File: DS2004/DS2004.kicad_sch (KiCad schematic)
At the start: 24 parts, among them U1 plot_i2, U2 plot_i2, U3 plot_i2, U4 plot_i2, U5 plot_i2, U6 plot_i2, U7 plot_i2, U8 plot_i2, X1 DS2004

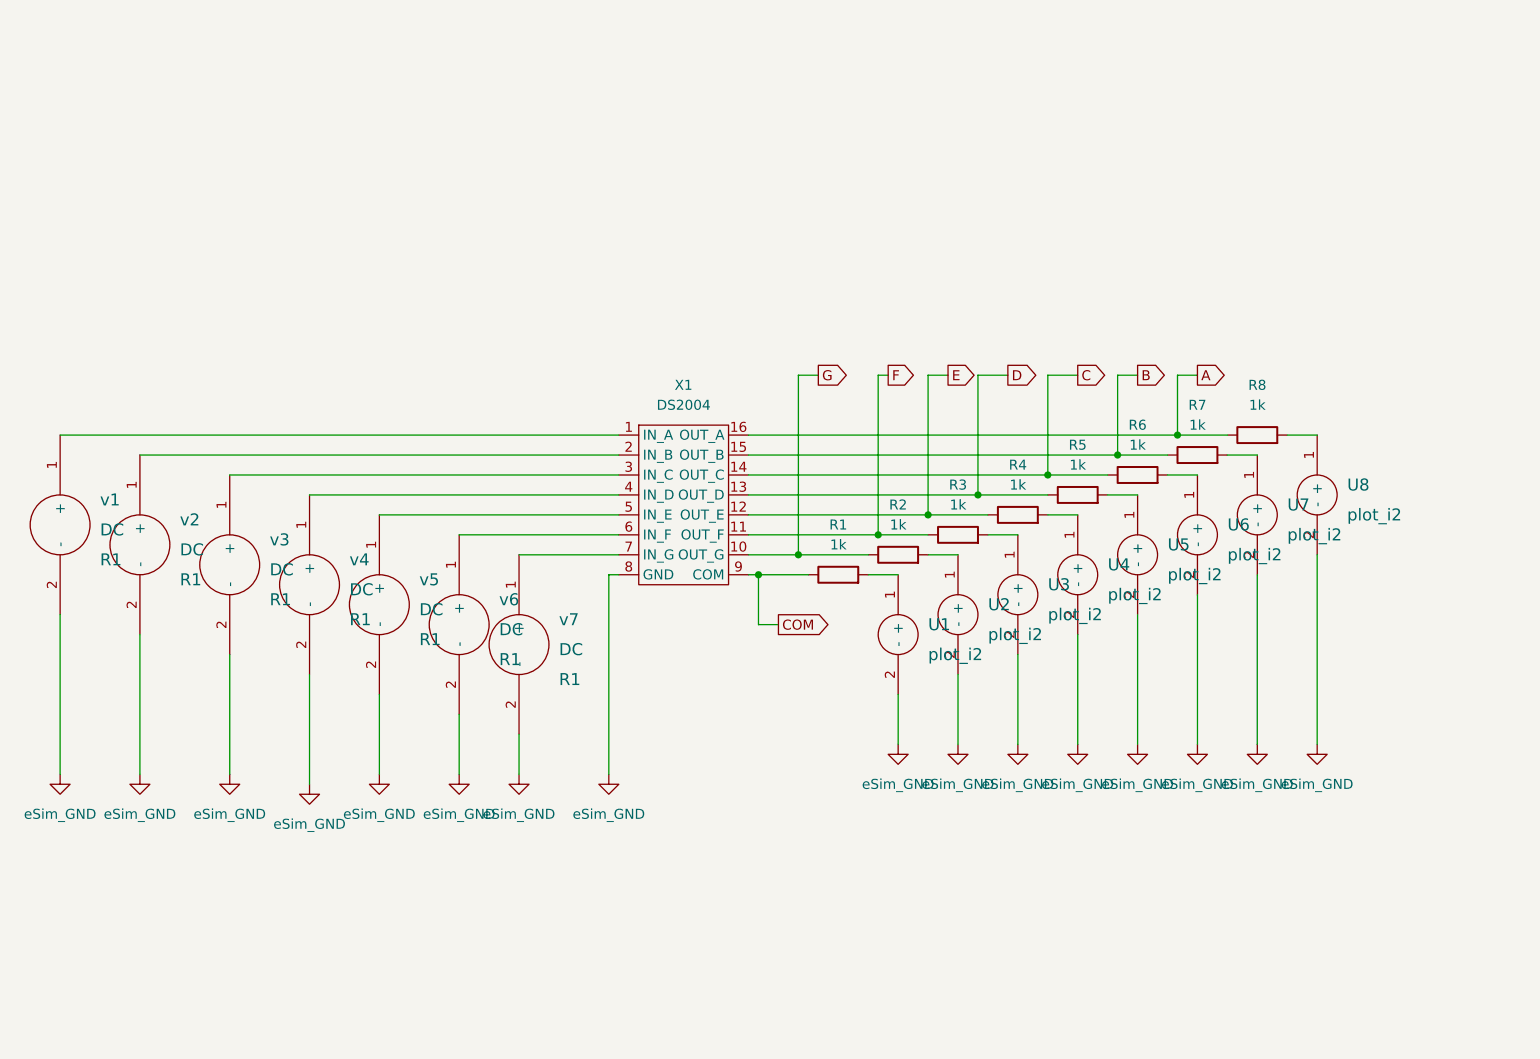
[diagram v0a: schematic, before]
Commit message: IC circuit of DS2004
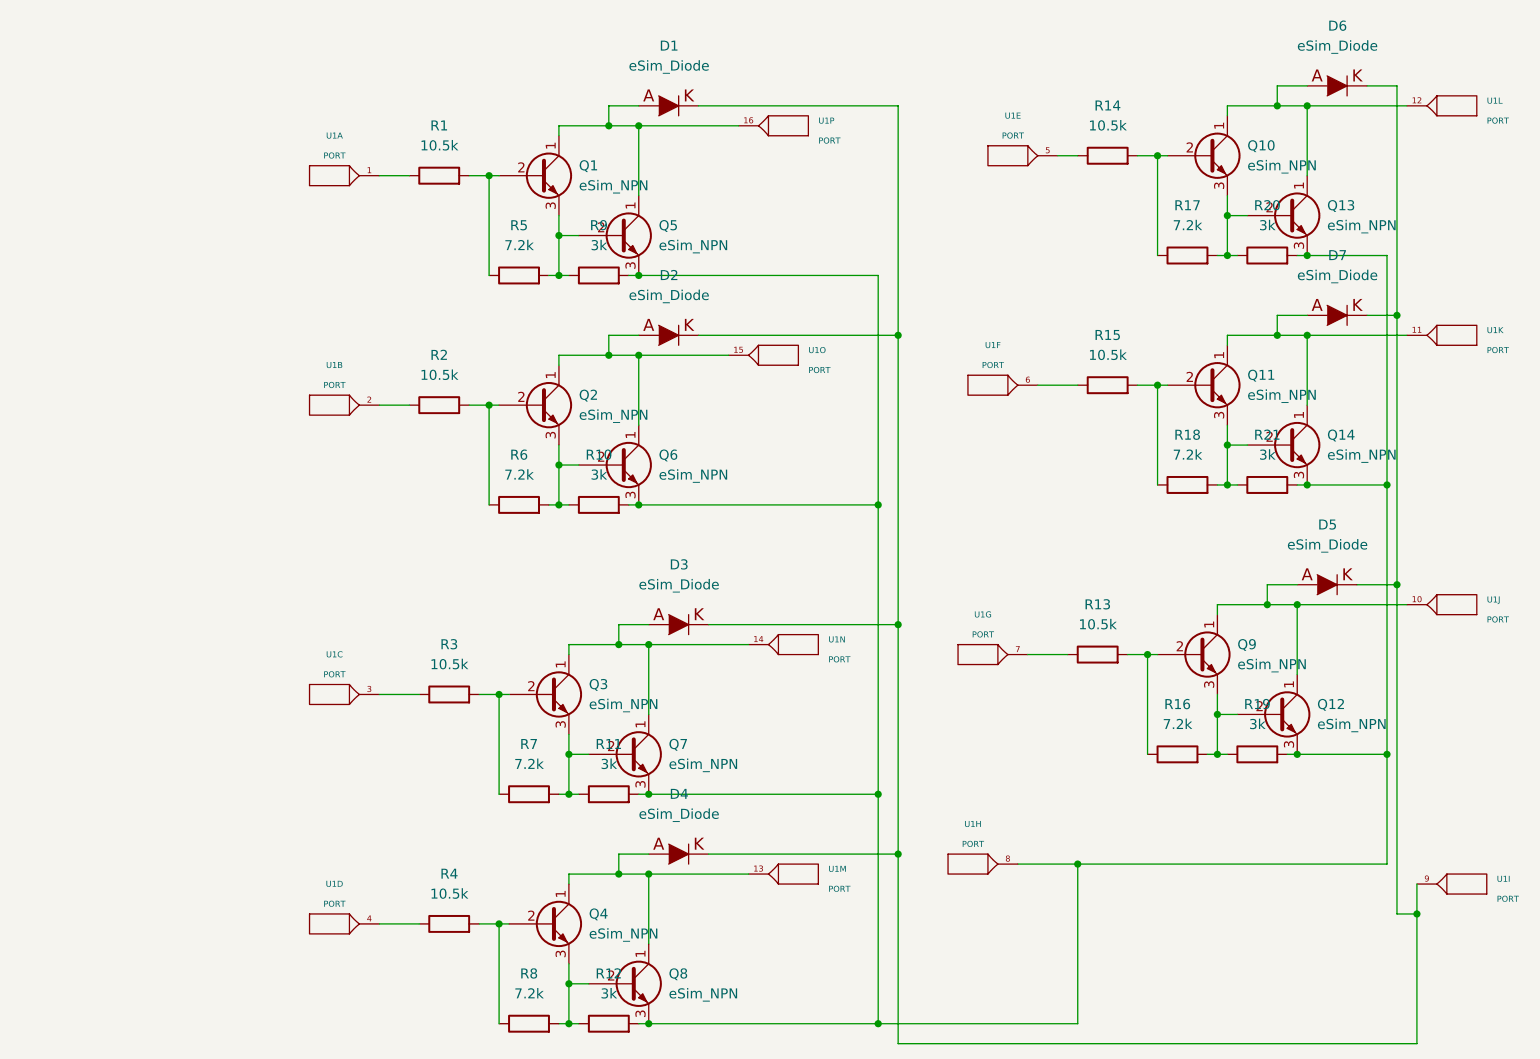
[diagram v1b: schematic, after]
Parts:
- removed U1, U2, U3, U4, U5, U6, U7, U8: plot_i2, symbol eSim_Plot:plot_i2
- removed X1: DS2004, symbol eSim_Subckt:DS2004
- removed v1, v2, v3, v4, v5, v6, v7: DC, R1, symbol eSim_Sources:DC
- added D1, D2, D3, D4, D5, D6, D7: eSim_Diode, symbol eSim_Devices:eSim_Diode
- added Q1, Q10, Q11, Q12, Q13, Q14, Q2, Q3, Q4, Q5, Q6, Q7, Q8, Q9: eSim_NPN, symbol eSim_Devices:eSim_NPN
- added R10, R11, R12, R19, R20, R21, R9: 3k, symbol eSim_Devices:resistor
- added R13, R14, R15: 10.5k, symbol eSim_Devices:resistor
- added R16, R17, R18: 7.2k, symbol eSim_Devices:resistor
- added U1: PORT, symbol eSim_Miscellaneous:PORT
- R1, R2, R3, R4: value 1k -> 10.5k
- R5, R6, R7, R8: value 1k -> 7.2k
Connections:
- net A is gone; now on an unnamed net: R8.1
- net B is gone; now on an unnamed net: R7.1
- net C is gone; now on an unnamed net: R6.1
- net D is gone; now on an unnamed net: R5.1
- net at R6.2: now also Q2.3 (E), Q6.2 (B), R10.1
- net at R8.2: now also Q4.3 (E), Q8.2 (B), R12.1
- net at R1.2: now also Q1.2 (B)
- net at R3.2: now also Q3.2 (B)
- net at R2.2: now also Q2.2 (B)
- net at R7.2: now also Q3.3 (E), Q7.2 (B), R11.1
- net at R4.2: now also Q4.2 (B)
- net at R5.2: now also Q1.3 (E), Q5.2 (B), R9.1
- net COM: no longer names the net of R1.1
- net COM: now also U1.1
- net E: no longer names the net of R4.1
- net E: now also U1.4
- net F: no longer names the net of R3.1
- net F: now also U1.3
- net G: no longer names the net of R2.1
- net G: now also U1.2
- new net: Q10.2 (B), R14.2, R17.1
- new net: Q10.3 (E), Q13.2 (B), R17.2, R20.1
- new net: Q12.3 (E), Q13.3 (E), Q14.3 (E), Q5.3 (E), Q6.3 (E), Q7.3 (E), Q8.3 (E), R10.2, R11.2, R12.2, R19.2, R20.2, R21.2, R9.2, U1.8
- new net: Q11.2 (B), R15.2, R18.1
- new net: Q11.3 (E), Q14.2 (B), R18.2, R21.1
- new net: D7.1 (A), Q11.1 (C), Q14.1 (C), U1.11
- new net: D1.2 (K), D2.2 (K), D3.2 (K), D4.2 (K), D5.2 (K), D6.2 (K), D7.2 (K), U1.9
- new net: D5.1 (A), Q12.1 (C), Q9.1 (C), U1.10
- new net: D4.1 (A), Q4.1 (C), Q8.1 (C), U1.13
- new net: R14.1, U1.5
- new net: D1.1 (A), Q1.1 (C), Q5.1 (C), U1.16
- new net: D3.1 (A), Q3.1 (C), Q7.1 (C), U1.14
- new net: R15.1, U1.6
- new net: Q9.2 (B), R13.2, R16.1
- new net: Q12.2 (B), Q9.3 (E), R16.2, R19.1
- new net: R13.1, U1.7
- new net: D2.1 (A), Q2.1 (C), Q6.1 (C), U1.15
- new net: D6.1 (A), Q10.1 (C), Q13.1 (C), U1.12
